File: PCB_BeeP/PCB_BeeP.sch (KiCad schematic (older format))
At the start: 18 parts, among them J1 Conn_01x02, J2 Conn_01x04, J3 Conn_01x02, J4 Conn_01x02, J5 Conn_01x04, J6 Conn_01x04, J7 Conn_01x02, U1 LM7805_TO220, U2 TP4056, U3 LM7805_TO220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

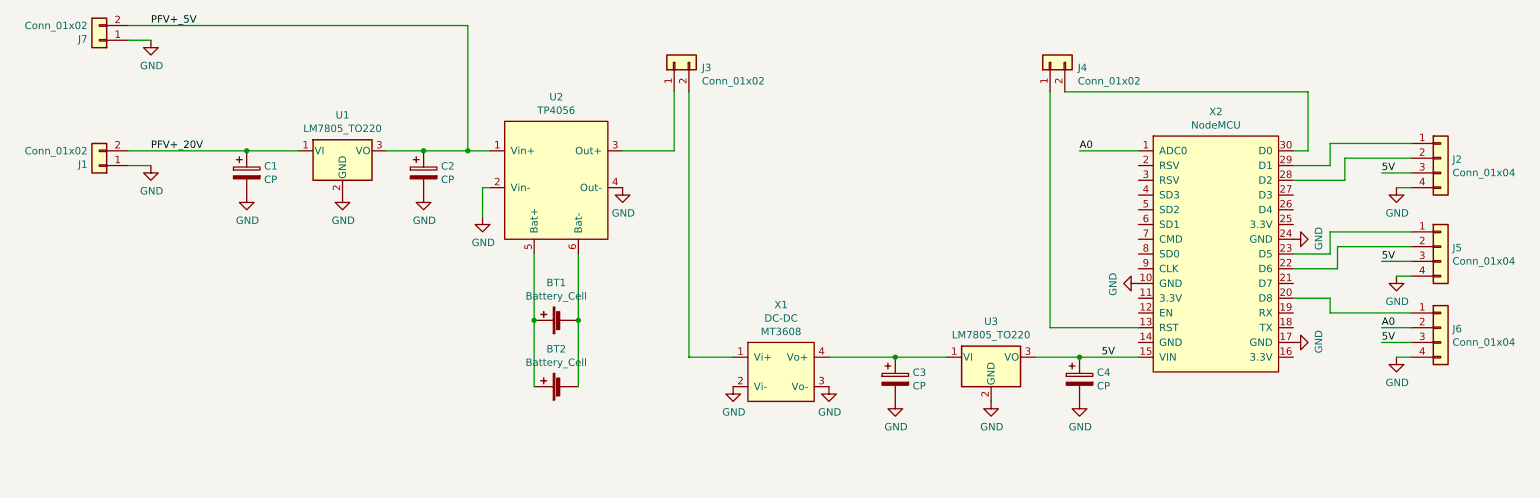
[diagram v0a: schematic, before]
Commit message: Placa abejas final - Isi
Agregados conectores porsiaca (GPS y 3G), pin de monitoreo de carga de la batería y modificación al lado de potencia (se asume que se tendrá para entonces un regulador MPPT para el panel FV, modificación a Julio Charger).
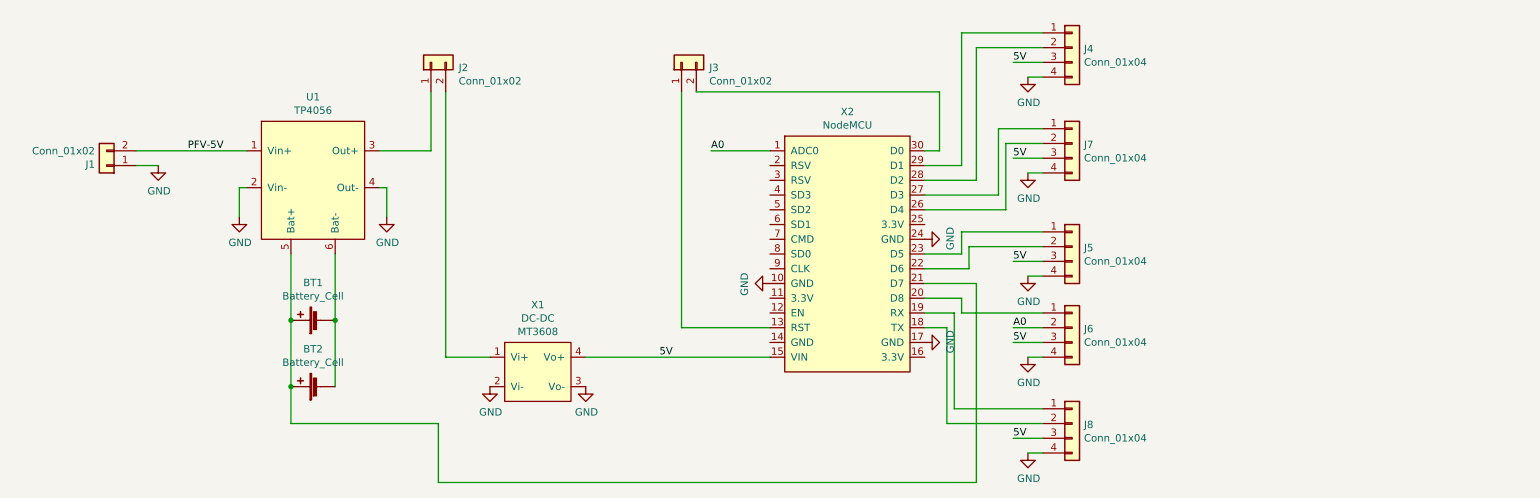
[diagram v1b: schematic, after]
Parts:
- removed C1, C2, C3, C4: CP, Capacitor_SMD:C_0603_1608Metric, symbol Device:CP
- removed J1: Conn_01x02, IoWLabsConnectors:Tb-2x1-5p-TH-V, symbol Connector_Generic:Conn_01x02
- removed U1, U3: LM7805_TO220, Package_TO_SOT_THT:TO-220-3_Vertical, symbol Regulator_Linear:LM7805_TO220
- added J7, J8: Conn_01x04, Connector_JST:JST_EH_B4B-EH-A_1x04_P2.50mm_Vertical, symbol Connector_Generic:Conn_01x04
- renumbered J7 to J1, J3 to J2, J4 to J3, J2 to J4, U2 to U1
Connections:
- net 5V: now also X1.4 (Vo+), J7.3 (Pin_3), J8.3 (Pin_3)
- net GND: now also J7.4 (Pin_4), J8.4 (Pin_4)
- net at X2.18 (TX): now also J8.2 (Pin_2)
- net at X2.19 (RX): now also J8.1 (Pin_1)
- net at X2.21 (D7): now also BT1.1 (+), BT2.1 (+), U1.5 (Bat+)
- net at X2.26 (D4): now also J7.2 (Pin_2)
- net at X2.27 (D3): now also J7.1 (Pin_1)
- net PFV+_5V renamed PFV-5V
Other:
- moved on the sheet: BT1, BT2, J1, J2, J3, J4, J5, J6, U1, X1, X2
